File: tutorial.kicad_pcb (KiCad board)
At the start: 2 copper layers, 75 x 50 mm, 59 parts, among them J1 Conn_01x04_Socket, J2 Conn_01x02_Pin, J5 USB_C_Receptacle, J7 Conn_01x08_Socket, SW1 SW_SPDT, SW2 SW_Push, U1 AMS1117-3.3, U2 STM32F103C8T6, U3 MCP2542FD, Y2 ASCO

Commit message: silk screen
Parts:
- added G***: LOGO, LOGO, F.Cu at (121.3, 87.8)
- added G***: LOGO, LOGO, F.Cu at (76.2, 80.2)

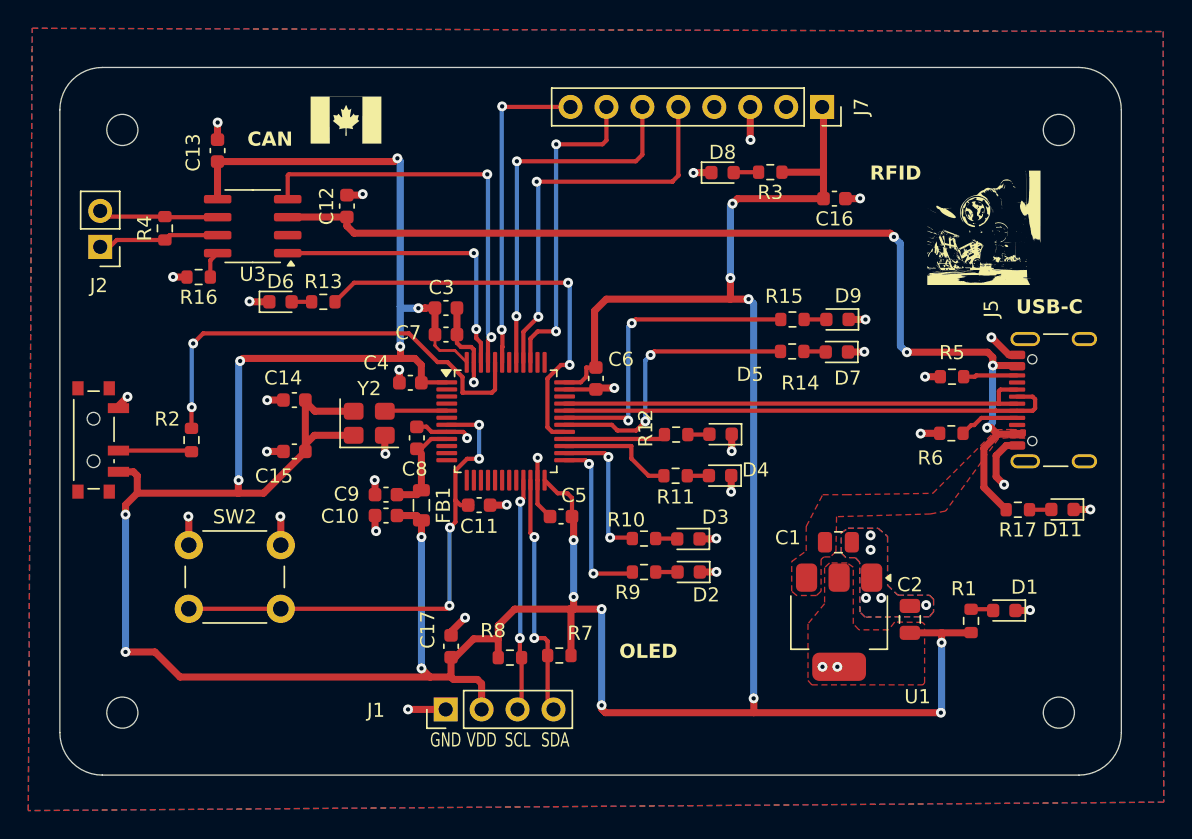
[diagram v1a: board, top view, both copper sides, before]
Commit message: Revised, added silkscreen
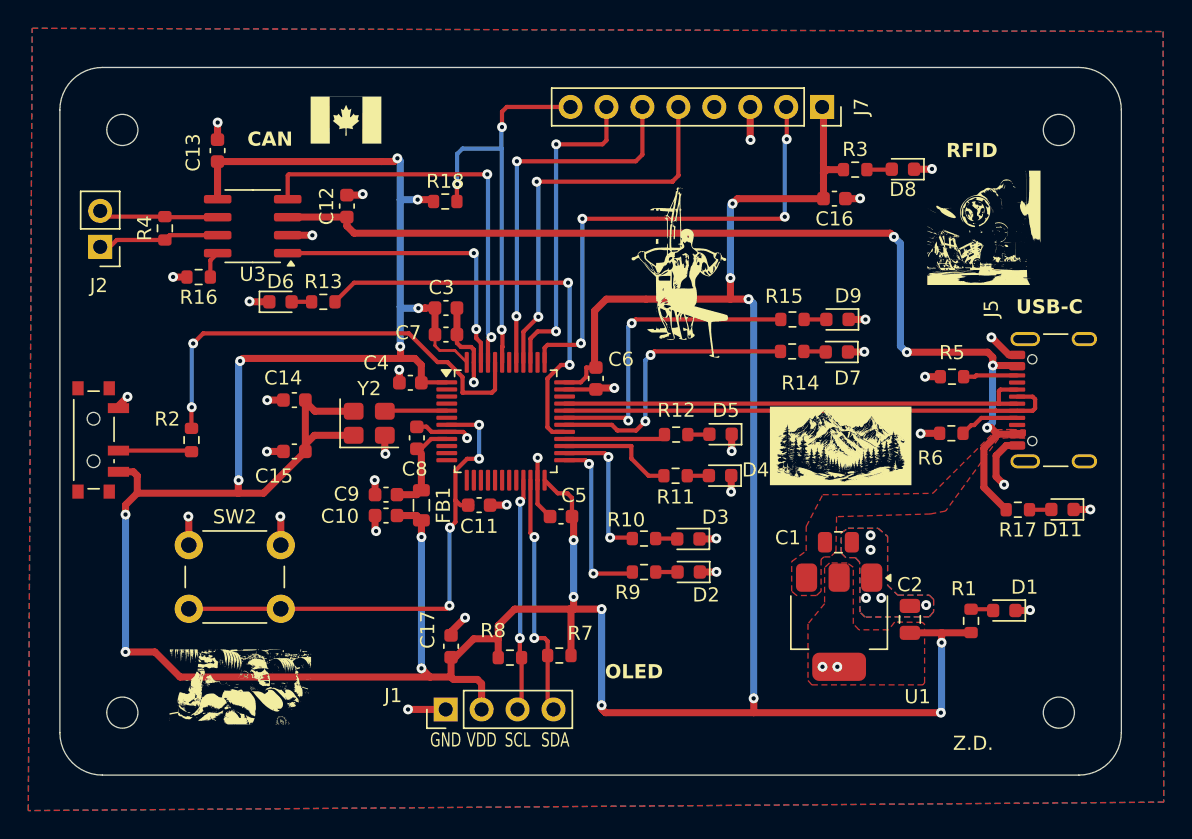
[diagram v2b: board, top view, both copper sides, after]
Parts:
- added G***: LOGO, LOGO, F.Cu at (68.8, 120.3)
- added G***: LOGO, LOGO, F.Cu at (99.9, 90.9)
- added G***: LOGO, LOGO, F.Cu at (111.2, 103.2)
- added R18: 1k5, Resistor_SMD:R_0603_1608Metric, F.Cu at (83.2, 86.0)
- moved D8 12.7 mm to (115.6, 83.7), turned to 180 degrees
- moved R3 6.00 mm to (112.2, 83.7), turned to 0 degrees
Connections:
- J7 pad 2: unconnected-(J7-Pin_2-Pad2) -> /RFID_RST
- U2 pad 37: unconnected-(U2-PA14-Pad37) -> /RFID_RST
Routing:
- net /RFID_RST: track 0.00 -> 34.8 mm, vias 0 -> 4
- net /RFID_SDA: track 23.0 -> 29.5 mm, vias 2 -> 3
- net GND: track 62.7 -> 64.5 mm, vias 40 -> 41
- net +3.3V: track 285.9 -> 286.9 mm, vias 21 -> 22
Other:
- board text added: "Z.D."

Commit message: Fix RFID pinout
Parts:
- removed R18: 1k5, Resistor_SMD:R_0603_1608Metric
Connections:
- U2 pad 14: unconnected-(U2-PA4-Pad14) -> /RFID_SDA
- U2 pad 15: unconnected-(U2-PA5-Pad15) -> /RFID_SCK
- U2 pad 16: unconnected-(U2-PA6-Pad16) -> /MISO
- U2 pad 17: unconnected-(U2-PA7-Pad17) -> /MOSI
- U2 pad 39: /RFID_SCK -> unconnected-(U2-PB3-Pad39)
- U2 pad 40: /MISO -> unconnected-(U2-PB4-Pad40)
- U2 pad 41: /MOSI -> unconnected-(U2-PB5-Pad41)
- U2 pad 43: /RFID_SDA -> unconnected-(U2-PB7-Pad43)
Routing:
- net /RFID_SCK: track 23.0 -> 34.0 mm, vias 2 -> 4
- net /MOSI: track 26.7 -> 36.7 mm
- net /MISO: track 28.3 -> 37.9 mm
- net /RFID_SDA: track 29.5 -> 32.7 mm, vias 3 -> 2
- net +3.3V: track 286.9 -> 284.5 mm, vias 22 -> 21
- net /NRST: vias 4 -> 3
